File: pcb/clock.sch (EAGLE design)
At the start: 17 parts, among them IC1 74AHCT125, U1 ESP-01, U2 LD1117V33

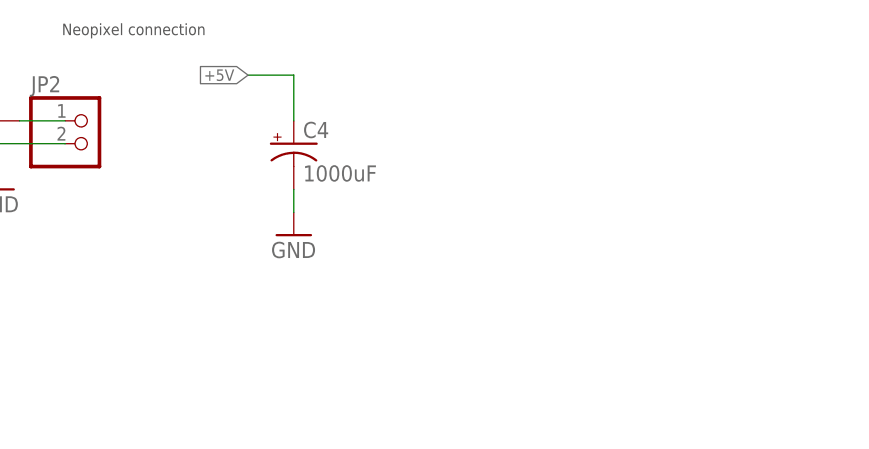
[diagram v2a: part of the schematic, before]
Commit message: Improved layout to make room for light sensor
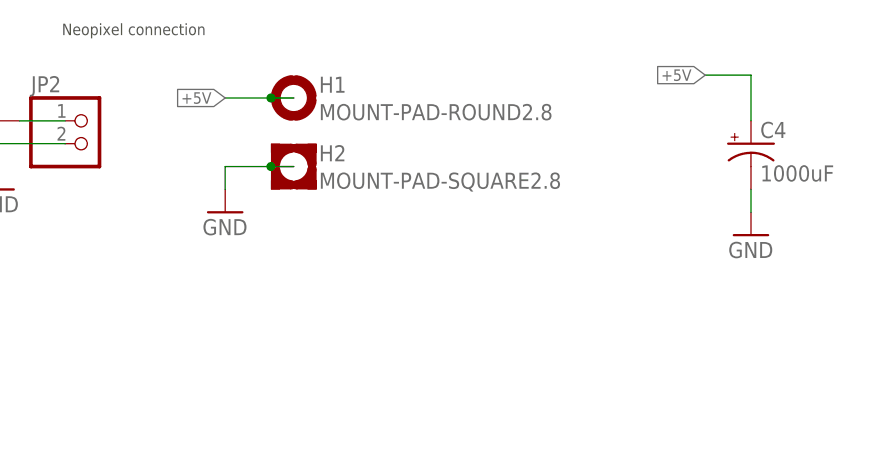
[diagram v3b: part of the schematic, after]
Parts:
- added H1: MOUNT-PAD-ROUND2.8, holes:MOUNT-PAD-ROUND2.8
- added H2: MOUNT-PAD-SQUARE2.8, holes:MOUNT-PAD-SQUARE2.8
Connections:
- net +5V: now also H1.MOUNT
- net GND: now also H2.MOUNT
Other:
- moved on the sheet: C4
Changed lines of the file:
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@@
 <part name="P+3" library="supply1" deviceset="VCC" device=""/>
 <part name="R6" library="rcl" deviceset="R-US_" device="0207/10" value="10K"/>
+<part name="H1" library="holes" deviceset="MOUNT-PAD-ROUND" device="2.8" value="MOUNT-PAD-ROUND2.8"/>
+<part name="H2" library="holes" deviceset="MOUNT-PAD-SQUARE" device="2.8"/>
+<part name="GND11" library="supply1" deviceset="GND" device=""/>
 </parts>
 <sheets>
@@
 <instance part="GND4" gate="1" x="27.94" y="139.7"/>
 <instance part="R1" gate="G$1" x="142.24" y="160.02"/>
-<instance part="C4" gate="G$1" x="177.8" y="157.48"/>
-<instance part="GND5" gate="1" x="177.8" y="147.32"/>
+<instance part="C4" gate="G$1" x="228.6" y="157.48"/>
+<instance part="GND5" gate="1" x="228.6" y="147.32"/>
 <instance part="JP2" gate="G$1" x="154.94" y="157.48"/>
 <instance part="GND6" gate="1" x="144.78" y="152.4"/>
@@
 <instance part="P+3" gate="VCC" x="91.44" y="53.34"/>
 <instance part="R6" gate="G$1" x="91.44" y="43.18" rot="R90"/>
+<instance part="H1" gate="G$1" x="177.8" y="162.56"/>
+<instance part="H2" gate="G$1" x="177.8" y="154.94"/>
+<instance part="GND11" gate="1" x="170.18" y="149.86"/>
 </instances>
 <busses>
@@
 <segment>
 <pinref part="C4" gate="G$1" pin="+"/>
-<wire x1="177.8" y1="160.02" x2="177.8" y2="165.1" width="0.1524" layer="91"/>
-<wire x1="177.8" y1="165.1" x2="172.72" y2="165.1" width="0.1524" layer="91"/>
-<label x="172.72" y="165.1" size="1.27" layer="95" rot="R180" xref="yes"/>
+<wire x1="228.6" y1="160.02" x2="228.6" y2="165.1" width="0.1524" layer="91"/>
+<wire x1="228.6" y1="165.1" x2="223.52" y2="165.1" width="0.1524" layer="91"/>
+<label x="223.52" y="165.1" size="1.27" layer="95" rot="R180" xref="yes"/>
 </segment>
 <segment>
@@
 <pinref part="IC1" gate="G$1" pin="14"/>
 <wire x1="228.6" y1="99.06" x2="231.14" y2="99.06" width="0.1524" layer="91"/>
+</segment>
+<segment>
+<wire x1="177.8" y1="162.56" x2="175.26" y2="162.56" width="0.1524" layer="91"/>
+<label x="170.18" y="162.56" size="1.27" layer="95" rot="R180" xref="yes"/>
+<pinref part="H1" gate="G$1" pin="MOUNT"/>
+<wire x1="175.26" y1="162.56" x2="170.18" y2="162.56" width="0.1524" layer="91"/>
+<junction x="175.26" y="162.56"/>
 </segment>
 </net>
@@
 <segment>
 <pinref part="C4" gate="G$1" pin="-"/>
-<wire x1="177.8" y1="152.4" x2="177.8" y2="149.86" width="0.1524" layer="91"/>
+<wire x1="228.6" y1="152.4" x2="228.6" y2="149.86" width="0.1524" layer="91"/>
 <pinref part="GND5" gate="1" pin="GND"/>
 </segment>
@@
 <pinref part="GND10" gate="1" pin="GND"/>
 </segment>
+<segment>
+<wire x1="177.8" y1="154.94" x2="175.26" y2="154.94" width="0.1524" layer="91"/>
+<wire x1="175.26" y1="154.94" x2="170.18" y2="154.94" width="0.1524" layer="91"/>
+<wire x1="170.18" y1="154.94" x2="170.18" y2="152.4" width="0.1524" layer="91"/>
+<pinref part="GND11" gate="1" pin="GND"/>
+<pinref part="H2" gate="G$1" pin="MOUNT"/>
+<junction x="175.26" y="154.94"/>
+</segment>
 </net>

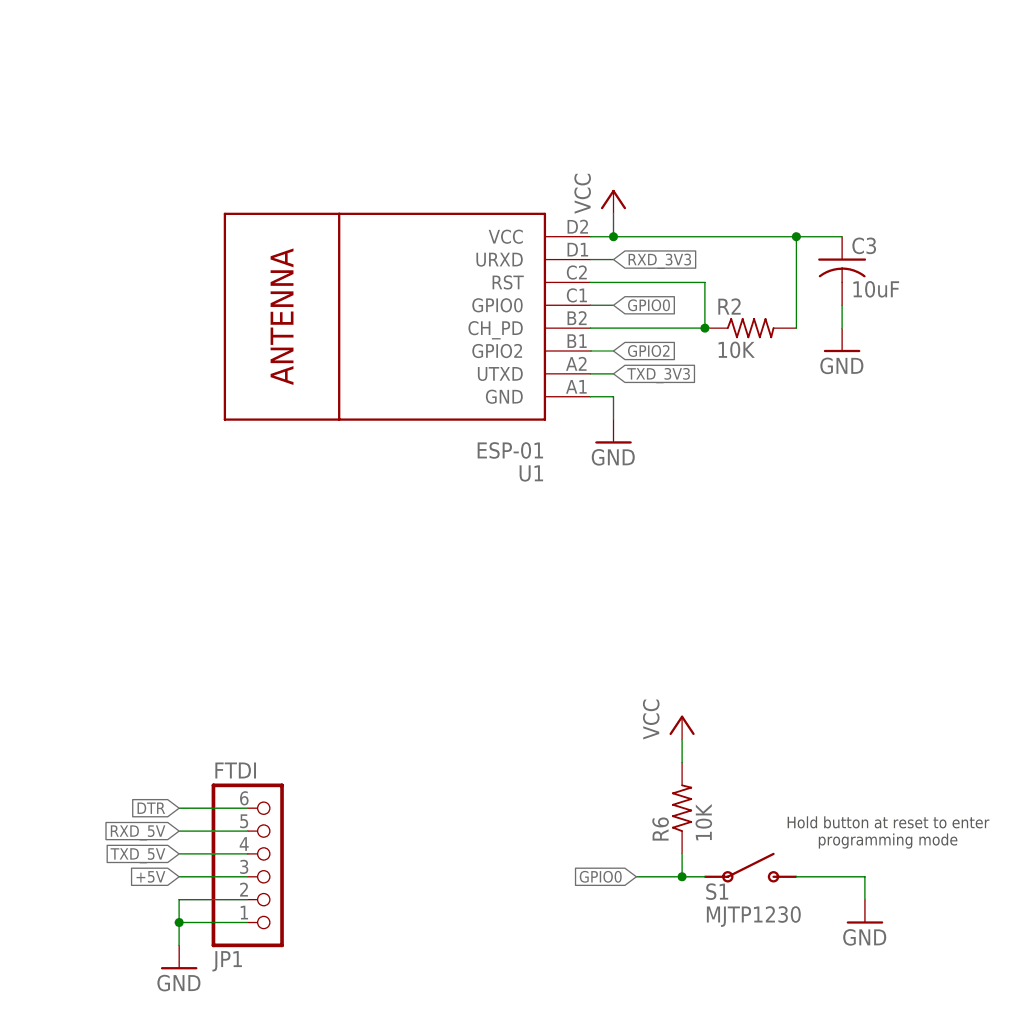
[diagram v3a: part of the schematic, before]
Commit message: Added RP diode, tweaked layout
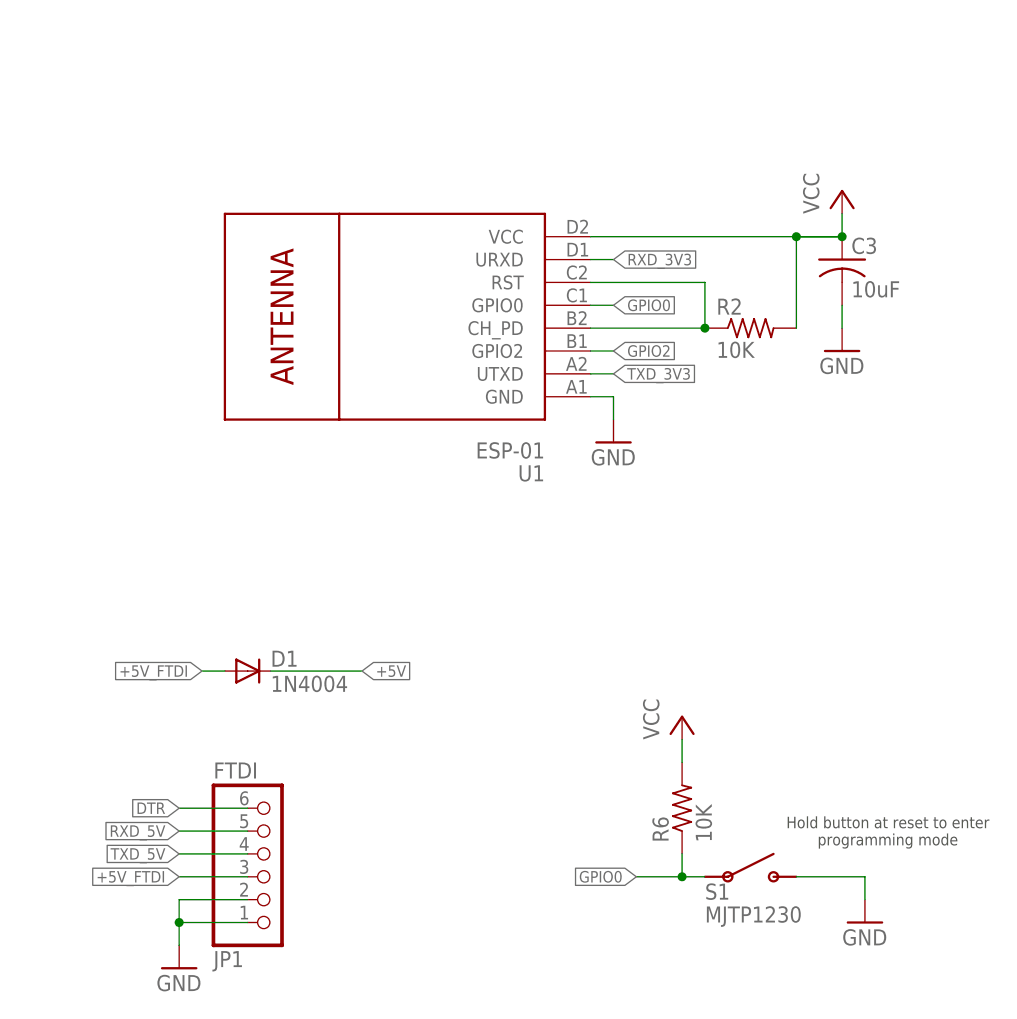
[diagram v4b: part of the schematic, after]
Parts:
- added D1: 1N4004, diode:1N4004
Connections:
- new net +5V_FTDI: D1.A, JP1.3
- net +5V: now also D1.C; no longer JP1.3
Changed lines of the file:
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@@
 <part name="H2" library="holes" deviceset="MOUNT-PAD-SQUARE" device="2.8"/>
 <part name="GND11" library="supply1" deviceset="GND" device=""/>
+<part name="D1" library="diode" deviceset="1N4004" device=""/>
 </parts>
 <sheets>
@@
 <instance part="GND1" gate="1" x="60.96" y="137.16"/>
 <instance part="P+1" gate="VCC" x="78.74" y="154.94"/>
-<instance part="P+2" gate="VCC" x="83.82" y="111.76"/>
+<instance part="P+2" gate="VCC" x="109.22" y="111.76"/>
 <instance part="GND2" gate="1" x="83.82" y="83.82"/>
 <instance part="C1" gate="G$1" x="45.72" y="144.78"/>
@@
 <instance part="H2" gate="G$1" x="177.8" y="154.94"/>
 <instance part="GND11" gate="1" x="170.18" y="149.86"/>
+<instance part="D1" gate="1" x="43.18" y="58.42"/>
 </instances>
 <busses>
@@
 </segment>
 <segment>
-<pinref part="JP1" gate="A" pin="3"/>
-<wire x1="43.18" y1="35.56" x2="35.56" y2="35.56" width="0.1524" layer="91"/>
-<label x="35.56" y="35.56" size="1.27" layer="95" rot="MR0" xref="yes"/>
-</segment>
-<segment>
 <pinref part="C4" gate="G$1" pin="+"/>
 <wire x1="228.6" y1="160.02" x2="228.6" y2="165.1" width="0.1524" layer="91"/>
@@
 <wire x1="175.26" y1="162.56" x2="170.18" y2="162.56" width="0.1524" layer="91"/>
 <junction x="175.26" y="162.56"/>
+</segment>
+<segment>
+<pinref part="D1" gate="1" pin="C"/>
+<wire x1="45.72" y1="58.42" x2="55.88" y2="58.42" width="0.1524" layer="91"/>
+<label x="55.88" y="58.42" size="1.27" layer="95" xref="yes"/>
 </segment>
 </net>
@@
 <pinref part="U1" gate="G$1" pin="VCC"/>
 <pinref part="P+2" gate="VCC" pin="VCC"/>
-<wire x1="81.28" y1="106.68" x2="83.82" y2="106.68" width="0.1524" layer="91"/>
-<wire x1="83.82" y1="106.68" x2="83.82" y2="109.22" width="0.1524" layer="91"/>
+<wire x1="81.28" y1="106.68" x2="109.22" y2="106.68" width="0.1524" layer="91"/>
+<wire x1="109.22" y1="106.68" x2="109.22" y2="109.22" width="0.1524" layer="91"/>
 <pinref part="C3" gate="G$1" pin="1"/>
-<wire x1="83.82" y1="106.68" x2="104.14" y2="106.68" width="0.1524" layer="91"/>
-<junction x="83.82" y="106.68"/>
+<junction x="109.22" y="106.68"/>
 <pinref part="R2" gate="G$1" pin="2"/>
 <wire x1="104.14" y1="106.68" x2="109.22" y2="106.68" width="0.1524" layer="91"/>
@@
 </segment>
 </net>
+<net name="+5V_FTDI" class="0">
+<segment>
+<pinref part="JP1" gate="A" pin="3"/>
+<wire x1="43.18" y1="35.56" x2="35.56" y2="35.56" width="0.1524" layer="91"/>
+<label x="35.56" y="35.56" size="1.27" layer="95" rot="R180" xref="yes"/>
+</segment>
+<segment>
+<pinref part="D1" gate="1" pin="A"/>
+<wire x1="40.64" y1="58.42" x2="38.1" y2="58.42" width="0.1524" layer="91"/>
+<label x="38.1" y="58.42" size="1.27" layer="95" rot="R180" xref="yes"/>
+</segment>
+</net>

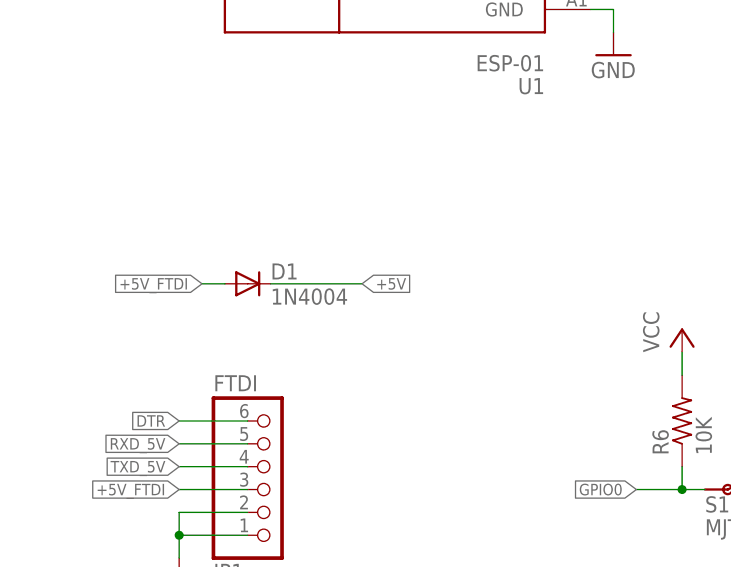
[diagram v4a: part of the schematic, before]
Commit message: Replaced 1N4004 with 1N5817
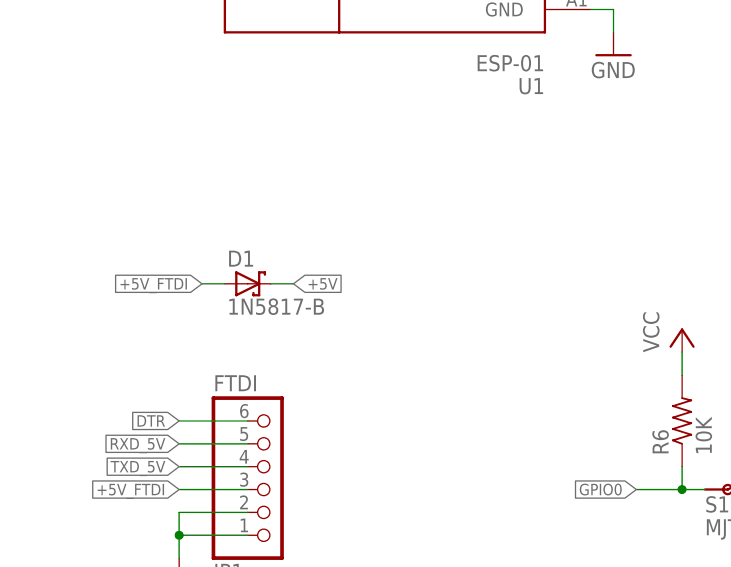
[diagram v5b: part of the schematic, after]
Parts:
- D1: value 1N4004 -> 1N5817-B; device diode:1N4004 -> diode:1N5817-B
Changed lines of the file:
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@@
 <part name="H2" library="holes" deviceset="MOUNT-PAD-SQUARE" device="2.8"/>
 <part name="GND11" library="supply1" deviceset="GND" device=""/>
-<part name="D1" library="diode" deviceset="1N4004" device=""/>
+<part name="D1" library="diode" deviceset="1N581*" device="" technology="7-B"/>
 </parts>
 <sheets>
@@
 <instance part="H2" gate="G$1" x="177.8" y="154.94"/>
 <instance part="GND11" gate="1" x="170.18" y="149.86"/>
-<instance part="D1" gate="1" x="43.18" y="58.42"/>
+<instance part="D1" gate="G$1" x="43.18" y="58.42"/>
 </instances>
 <busses>
@@
 </segment>
 <segment>
-<pinref part="D1" gate="1" pin="C"/>
-<wire x1="45.72" y1="58.42" x2="55.88" y2="58.42" width="0.1524" layer="91"/>
-<label x="55.88" y="58.42" size="1.27" layer="95" xref="yes"/>
+<wire x1="45.72" y1="58.42" x2="48.26" y2="58.42" width="0.1524" layer="91"/>
+<label x="48.26" y="58.42" size="1.27" layer="95" xref="yes"/>
+<pinref part="D1" gate="G$1" pin="C"/>
 </segment>
 </net>
@@
 </segment>
 <segment>
-<pinref part="D1" gate="1" pin="A"/>
 <wire x1="40.64" y1="58.42" x2="38.1" y2="58.42" width="0.1524" layer="91"/>
 <label x="38.1" y="58.42" size="1.27" layer="95" rot="R180" xref="yes"/>
-</segment>
-</net>
+<pinref part="D1" gate="G$1" pin="A"/>
+</segment>
+</net>
